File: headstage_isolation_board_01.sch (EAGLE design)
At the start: 55 parts, among them J1 DC_POWER_JACK-PJ-102AH

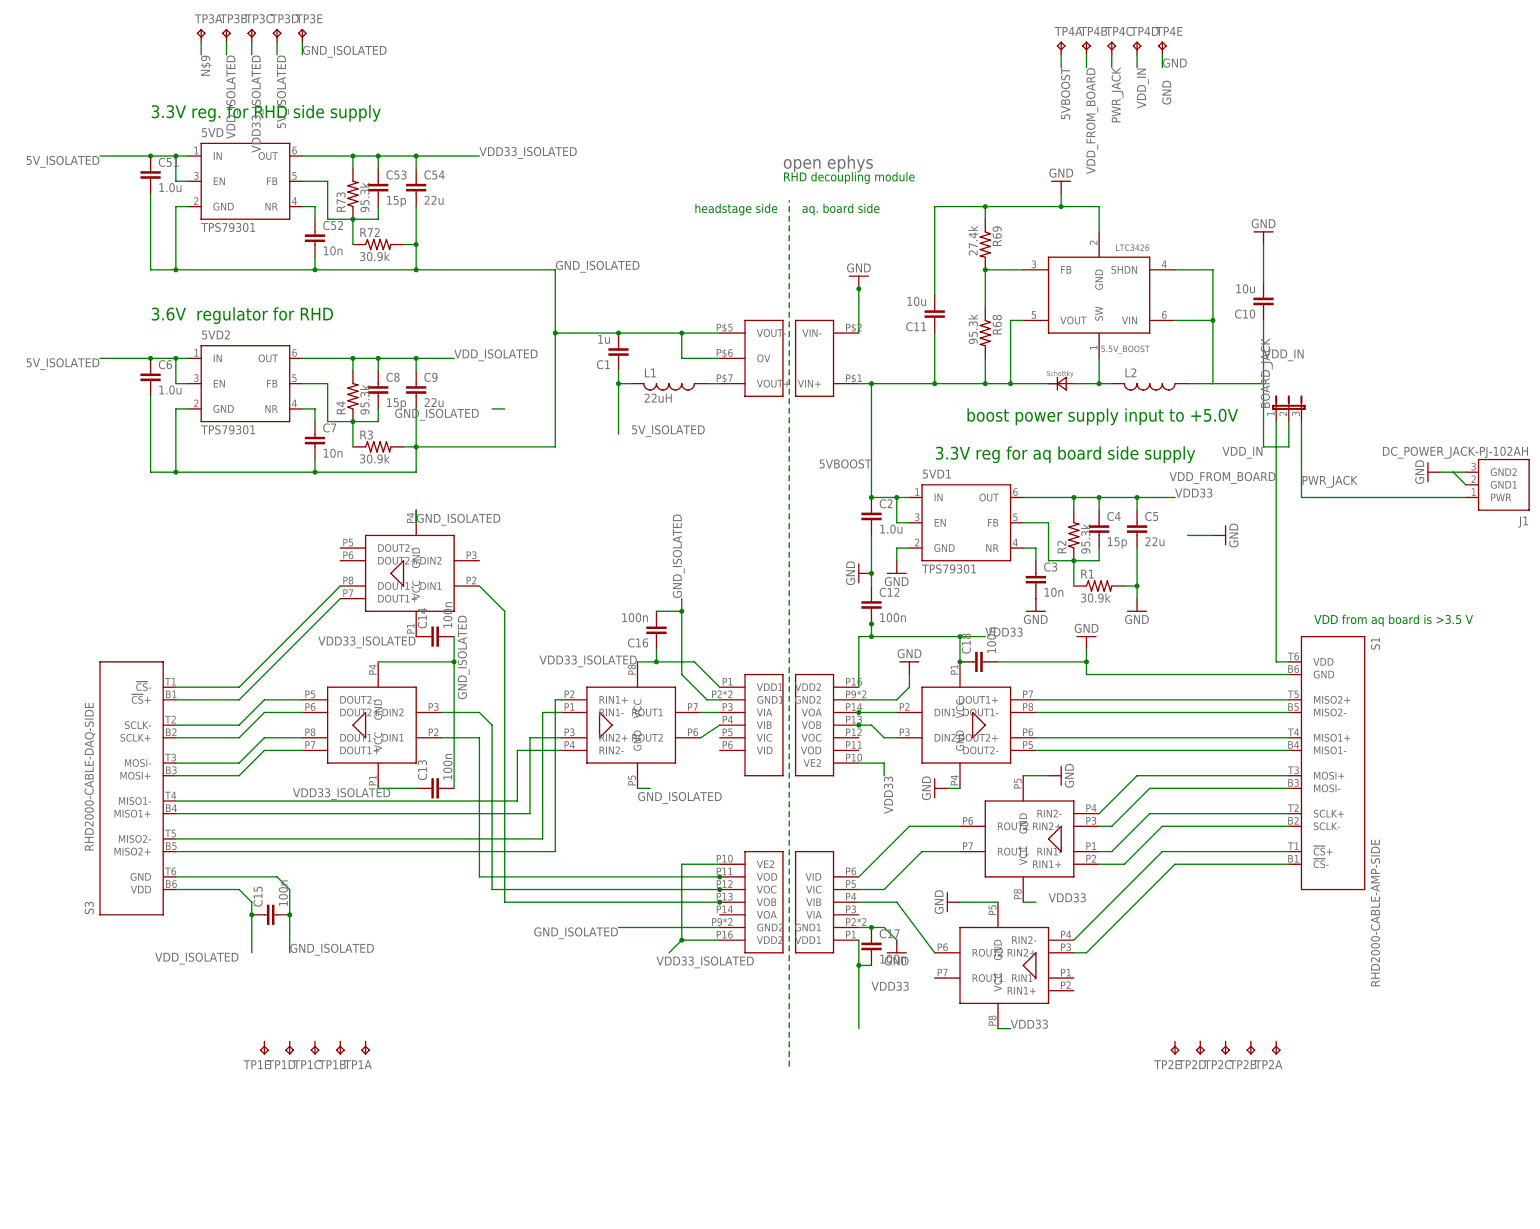
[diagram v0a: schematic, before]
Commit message: added all test points
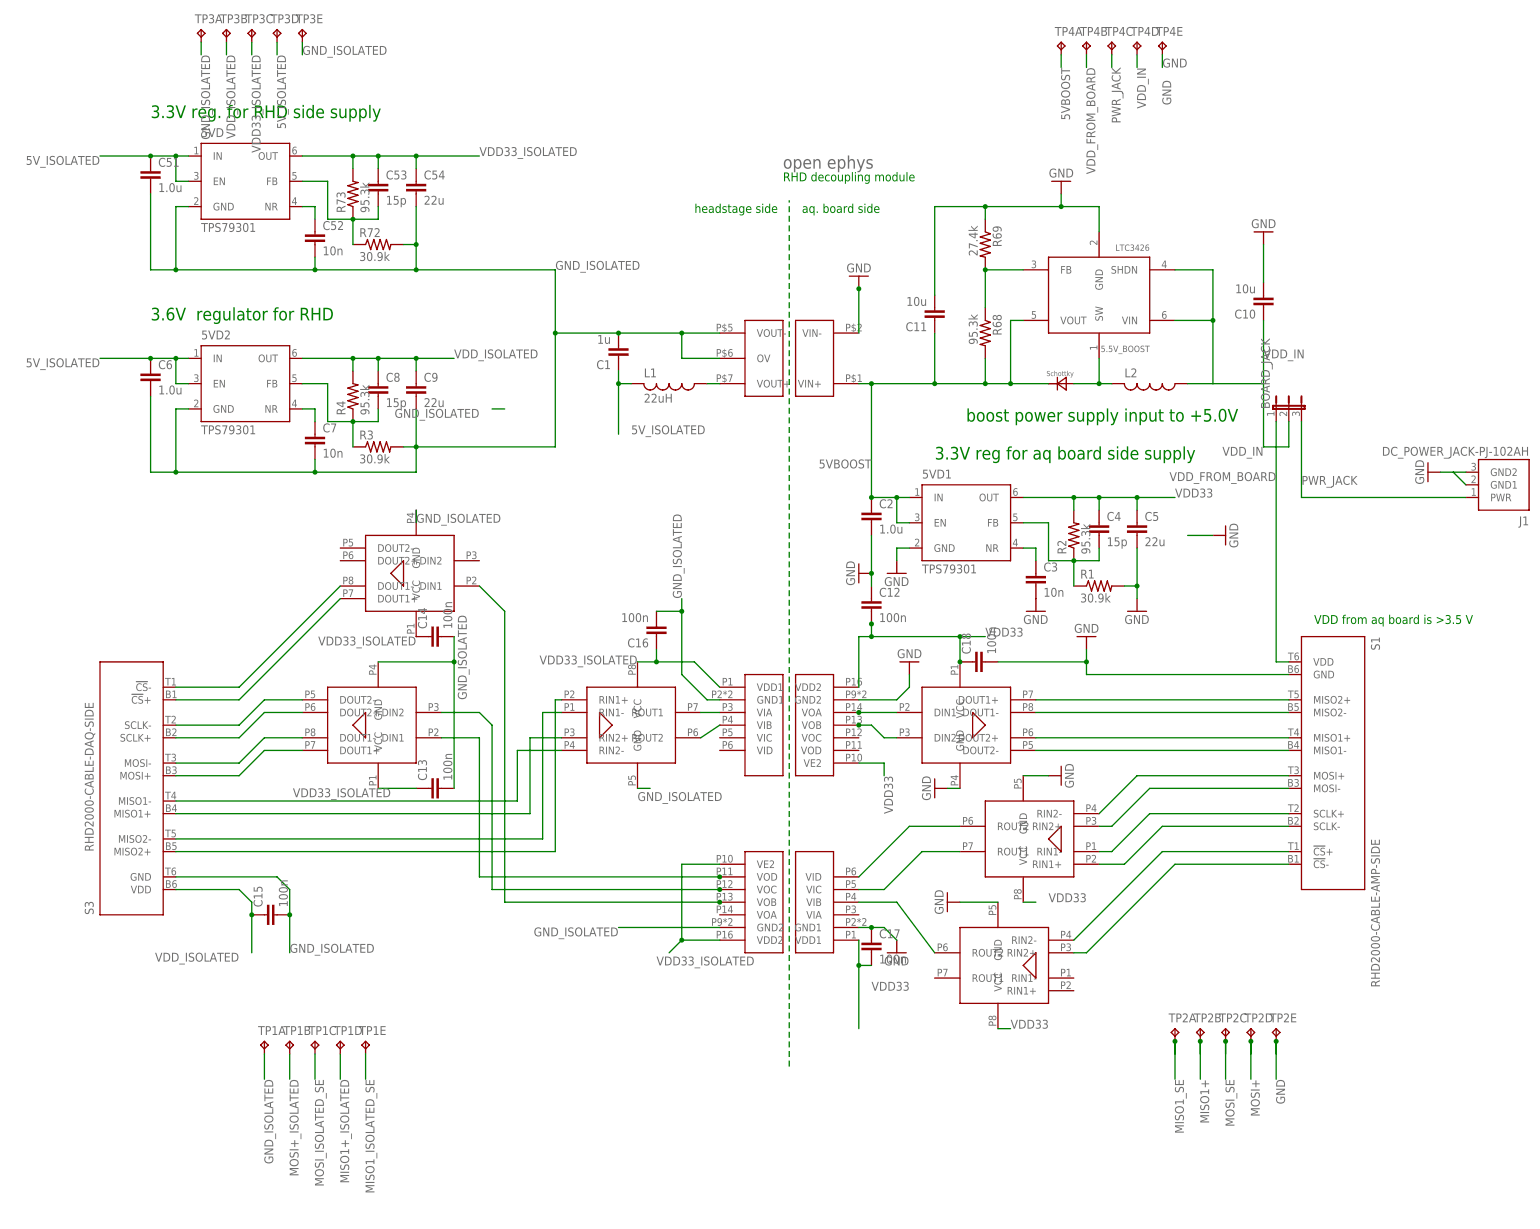
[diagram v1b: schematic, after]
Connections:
- net N$26 renamed SCLK_SE
- net N$27 renamed CS_SE
- net N$29 renamed SCLK_ISOLATED_SE
- net N$30 renamed CS_ISOLATED_SE
- net N$5 renamed MISO2_SE
- net N$7 renamed MISO2_ISOLATED_SE
- removed net N$25: U$2.VID, U$7.ROUT2
- removed net N$28: U$2.VOD, U$5.DIN1
- removed net N$6: U$10.VOB, U$4.DIN2
- removed net N$8: U$10.VIB, U$6.ROUT2
- removed net N$9: TP3A.TP
- new net MISO1_ISOLATED_SE: TP1E.TP, U$10.VIB, U$6.ROUT2
- new net MISO1_SE: TP2A.TP, U$10.VOB, U$4.DIN2
- new net MOSI_ISOLATED_SE: TP1C.TP, U$2.VOD, U$5.DIN1
- new net MOSI_SE: TP2C.TP, U$2.VID, U$7.ROUT2
- net GND: now also TP2E.TP
- net GND_ISOLATED: now also TP1A.TP, TP3A.TP
- net MISO1+: now also TP2B.TP
- net MISO1+_ISOLATED: now also TP1D.TP
- net MOSI+: now also TP2D.TP
- net MOSI+_ISOLATED: now also TP1B.TP
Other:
- moved on the sheet: TP1A, TP1B, TP1C, TP1D, TP1E, TP2A, TP2B, TP2C, TP2D, TP2E
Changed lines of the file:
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@@
 <part name="C18" library="RHD2000_eval_board" deviceset="C" device="_0603" value="100n"/>
 <part name="S3" library="RHD2000_eval_board" deviceset="RHD2000-CABLE-DAQ-SIDE" device=""/>
-<part name="TP1" library="testpad" deviceset="TP5" device="P5-25-13"/>
-<part name="TP2" library="testpad" deviceset="TP5" device="P5-25-13"/>
 <part name="TP3" library="testpad" deviceset="TP5" device="P5-25-13"/>
 <part name="TP4" library="testpad" deviceset="TP5" device="P5-25-13"/>
@@
 <part name="J1" library="RHD2000_eval_board" deviceset="DC_POWER_JACK" device="-PJ-102AH"/>
 <part name="GND12" library="supply1" deviceset="GND" device=""/>
+<part name="TP1" library="testpad" deviceset="TP5" device="P5-25-13"/>
+<part name="TP2" library="testpad" deviceset="TP5" device="P5-25-13"/>
 </parts>
 <sheets>
@@
 <instance part="C18" gate="C" x="99.06" y="-38.1" rot="R90"/>
 <instance part="S3" gate="A" x="-68.58" y="-63.5" rot="R270"/>
-<instance part="TP1" gate="A" x="-22.86" y="-116.84" rot="R180"/>
-<instance part="TP1" gate="B" x="-27.94" y="-116.84" rot="R180"/>
-<instance part="TP1" gate="C" x="-33.02" y="-116.84" rot="R180"/>
-<instance part="TP1" gate="D" x="-38.1" y="-116.84" rot="R180"/>
-<instance part="TP1" gate="E" x="-43.18" y="-116.84" rot="R180"/>
-<instance part="TP2" gate="A" x="160.02" y="-116.84" rot="R180"/>
-<instance part="TP2" gate="B" x="154.94" y="-116.84" rot="R180"/>
-<instance part="TP2" gate="C" x="149.86" y="-116.84" rot="R180"/>
-<instance part="TP2" gate="D" x="144.78" y="-116.84" rot="R180"/>
-<instance part="TP2" gate="E" x="139.7" y="-116.84" rot="R180"/>
 <instance part="TP3" gate="A" x="-55.88" y="88.9"/>
 <instance part="TP3" gate="B" x="-50.8" y="88.9"/>
@@
 <instance part="J1" gate="A" x="205.74" y="-2.54" rot="R180"/>
 <instance part="GND12" gate="1" x="190.5" y="0" rot="R270"/>
+<instance part="TP1" gate="A" x="-43.18" y="-114.3"/>
+<instance part="TP1" gate="B" x="-38.1" y="-114.3"/>
+<instance part="TP1" gate="C" x="-33.02" y="-114.3"/>
+<instance part="TP1" gate="D" x="-27.94" y="-114.3"/>
+<instance part="TP1" gate="E" x="-22.86" y="-114.3"/>
+<instance part="TP2" gate="A" x="139.7" y="-111.76"/>
+<instance part="TP2" gate="B" x="144.78" y="-111.76"/>
+<instance part="TP2" gate="C" x="149.86" y="-111.76"/>
+<instance part="TP2" gate="D" x="154.94" y="-111.76"/>
+<instance part="TP2" gate="E" x="160.02" y="-111.76"/>
 </instances>
 <busses>
@@
 <wire x1="111.76" y1="-53.34" x2="162.56" y2="-53.34" width="0.1524" layer="91"/>
 </segment>
+<segment>
+<wire x1="144.78" y1="-116.84" x2="144.78" y2="-114.3" width="0.1524" layer="91"/>
+<label x="144.78" y="-121.92" size="1.778" layer="95" rot="R270"/>
+<pinref part="TP2" gate="B" pin="TP"/>
+<wire x1="144.78" y1="-114.3" x2="144.78" y2="-121.92" width="0.1524" layer="91"/>
+<junction x="144.78" y="-114.3"/>
+</segment>
 </net>
 <net name="MISO1-" class="0">
@@
 </segment>
 </net>
-<net name="N$5" class="0">
+<net name="MISO2_SE" class="0">
 <segment>
 <pinref part="U$4" gate="G$1" pin="DIN1"/>
@@
 </segment>
 </net>
-<net name="N$6" class="0">
+<net name="MISO1_SE" class="0">
 <segment>
 <pinref part="U$4" gate="G$1" pin="DIN2"/>
@@
 <junction x="76.2" y="-50.8"/>
 </segment>
-</net>
-<net name="N$7" class="0">
+<segment>
+<wire x1="139.7" y1="-116.84" x2="139.7" y2="-114.3" width="0.1524" layer="91"/>
+<label x="139.7" y="-121.92" size="1.778" layer="95" rot="R270"/>
+<pinref part="TP2" gate="A" pin="TP"/>
+<wire x1="139.7" y1="-114.3" x2="139.7" y2="-121.92" width="0.1524" layer="91"/>
+<junction x="139.7" y="-114.3"/>
+</segment>
+</net>
+<net name="MISO2_ISOLATED_SE" class="0">
 <segment>
 <pinref part="U$6" gate="G$1" pin="ROUT1"/>
@@
 </segment>
 </net>
-<net name="N$8" class="0">
+<net name="MISO1_ISOLATED_SE" class="0">
 <segment>
 <pinref part="U$6" gate="G$1" pin="ROUT2"/>
 <wire x1="48.26" y1="-50.8" x2="44.45" y2="-53.34" width="0.1524" layer="91"/>
 <pinref part="U$10" gate="G$1" pin="VIB"/>
+</segment>
+<segment>
+<wire x1="-22.86" y1="-116.84" x2="-22.86" y2="-121.92" width="0.1524" layer="91"/>
+<label x="-22.86" y="-121.92" size="1.778" layer="95" rot="R270"/>
+<pinref part="TP1" gate="E" pin="TP"/>
 </segment>
 </net>
@@
 <pinref part="S3" gate="A" pin="MISO1+"/>
 </segment>
+<segment>
+<wire x1="-27.94" y1="-116.84" x2="-27.94" y2="-121.92" width="0.1524" layer="91"/>
+<label x="-27.94" y="-121.92" size="1.778" layer="95" rot="R270"/>
+<pinref part="TP1" gate="D" pin="TP"/>
+</segment>
 </net>
 <net name="MISO1-_ISOLATED" class="0">
@@
 <pinref part="U$7" gate="G$1" pin="RIN2-"/>
 </segment>
+<segment>
+<wire x1="154.94" y1="-116.84" x2="154.94" y2="-114.3" width="0.1524" layer="91"/>
+<label x="154.94" y="-121.92" size="1.778" layer="95" rot="R270"/>
+<pinref part="TP2" gate="D" pin="TP"/>
+<wire x1="154.94" y1="-114.3" x2="154.94" y2="-121.92" width="0.1524" layer="91"/>
+<junction x="154.94" y="-114.3"/>
+</segment>
 </net>
 <net name="CS-" class="0">
@@
 </segment>
 </net>
-<net name="N$28" class="0">
+<net name="MOSI_ISOLATED_SE" class="0">
 <segment>
 <wire x1="-7.62" y1="-53.34" x2="0" y2="-53.34" width="0.1524" layer="91"/>
@@
 <junction x="48.26" y="-81.28"/>
 </segment>
-</net>
-<net name="N$29" class="0">
+<segment>
+<wire x1="-33.02" y1="-116.84" x2="-33.02" y2="-121.92" width="0.1524" layer="91"/>
+<label x="-33.02" y="-121.92" size="1.778" layer="95" rot="R270"/>
+<pinref part="TP1" gate="C" pin="TP"/>
+</segment>
+</net>
+<net name="SCLK_ISOLATED_SE" class="0">
 <segment>
 <wire x1="48.26" y1="-83.82" x2="2.54" y2="-83.82" width="0.1524" layer="91"/>
@@
 </segment>
 </net>
-<net name="N$30" class="0">
+<net name="CS_ISOLATED_SE" class="0">
 <segment>
 <wire x1="48.26" y1="-86.36" x2="5.08" y2="-86.36" width="0.1524" layer="91"/>
@@
 <wire x1="-48.26" y1="-60.96" x2="-60.96" y2="-60.96" width="0.1524" layer="91"/>
 </segment>
-</net>
-<net name="N$25" class="0">
+<segment>
+<wire x1="-38.1" y1="-116.84" x2="-38.1" y2="-121.92" width="0.1524" layer="91"/>
+<label x="-38.1" y="-121.92" size="1.778" layer="95" rot="R270"/>
+<pinref part="TP1" gate="B" pin="TP"/>
+</segment>
+</net>
+<net name="MOSI_SE" class="0">
 <segment>
 <wire x1="76.2" y1="-81.28" x2="86.36" y2="-71.12" width="0.1524" layer="91"/>
@@
 <pinref part="U$2" gate="G$1" pin="VID"/>
 </segment>
-</net>
-<net name="N$26" class="0">
+<segment>
+<wire x1="149.86" y1="-116.84" x2="149.86" y2="-114.3" width="0.1524" layer="91"/>
+<label x="149.86" y="-121.92" size="1.778" layer="95" rot="R270"/>
+<pinref part="TP2" gate="C" pin="TP"/>
+<wire x1="149.86" y1="-114.3" x2="149.86" y2="-121.92" width="0.1524" layer="91"/>
+<junction x="149.86" y="-114.3"/>
+</segment>
+</net>
+<net name="SCLK_SE" class="0">
 <segment>
 <pinref part="U$7" gate="G$1" pin="ROUT1"/>
@@
 </segment>
 </net>
-<net name="N$27" class="0">
+<net name="CS_SE" class="0">
 <segment>
 <pinref part="U$8" gate="G$1" pin="ROUT2"/>
@@
 <label x="-35.56" y="83.82" size="1.778" layer="95"/>
 </segment>
+<segment>
+<wire x1="-43.18" y1="-116.84" x2="-43.18" y2="-121.92" width="0.1524" layer="91"/>
+<label x="-43.18" y="-121.92" size="1.778" layer="95" rot="R270"/>
+<pinref part="TP1" gate="A" pin="TP"/>
+</segment>
+<segment>
+<pinref part="TP3" gate="A" pin="TP"/>
+<wire x1="-55.88" y1="86.36" x2="-55.88" y2="83.82" width="0.1524" layer="91"/>
+<label x="-55.88" y="83.82" size="1.778" layer="95" rot="R270"/>
+</segment>
 </net>
 <net name="VDD_ISOLATED" class="0">
@@
 <wire x1="195.58" y1="0" x2="193.04" y2="0" width="0.1524" layer="91"/>
 <pinref part="GND12" gate="1" pin="GND"/>
+</segment>
+<segment>
+<wire x1="160.02" y1="-116.84" x2="160.02" y2="-114.3" width="0.1524" layer="91"/>
+<label x="160.02" y="-121.92" size="1.778" layer="95" rot="R270"/>
+<pinref part="TP2" gate="E" pin="TP"/>
+<wire x1="160.02" y1="-114.3" x2="160.02" y2="-121.92" width="0.1524" layer="91"/>
+<junction x="160.02" y="-114.3"/>
 </segment>
 </net>
@@
 </segment>
 </net>
-<net name="N$9" class="0">
-<segment>
-<pinref part="TP3" gate="A" pin="TP"/>
-<wire x1="-55.88" y1="86.36" x2="-55.88" y2="83.82" width="0.1524" layer="91"/>
-<label x="-55.88" y="83.82" size="1.778" layer="95" rot="R270"/>
-</segment>
-</net>

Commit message: added LVDS termination resistors
should fix bug #2
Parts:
- added R5, R6: 100, RHD2000_eval_board:R_0603
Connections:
- net MISO1+_ISOLATED: now also R6.1
- net MISO1-_ISOLATED: now also R6.2
- net MISO2+_ISOLATED: now also R5.1
- net MISO2-_ISOLATED: now also R5.2
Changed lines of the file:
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@@
 <part name="TP1" library="testpad" deviceset="TP5" device="P5-25-13"/>
 <part name="TP2" library="testpad" deviceset="TP5" device="P5-25-13"/>
+<part name="R5" library="RHD2000_eval_board" deviceset="R" device="_0603" value="100"/>
+<part name="R6" library="RHD2000_eval_board" deviceset="R" device="_0603" value="100"/>
 </parts>
 <sheets>
@@
 <instance part="TP2" gate="D" x="154.94" y="-111.76"/>
 <instance part="TP2" gate="E" x="160.02" y="-111.76"/>
+<instance part="R5" gate="R" x="-25.4" y="-81.28"/>
+<instance part="R6" gate="R" x="-12.7" y="-81.28"/>
 </instances>
 <busses>
@@
 <wire x1="16.51" y1="-48.26" x2="12.7" y2="-48.26" width="0.1524" layer="91"/>
 <wire x1="12.7" y1="-48.26" x2="12.7" y2="-73.66" width="0.1524" layer="91"/>
-<wire x1="12.7" y1="-73.66" x2="-60.96" y2="-73.66" width="0.1524" layer="91"/>
+<wire x1="12.7" y1="-73.66" x2="-20.32" y2="-73.66" width="0.1524" layer="91"/>
 <pinref part="S3" gate="A" pin="MISO2-"/>
+<pinref part="R5" gate="R" pin="2"/>
+<wire x1="-20.32" y1="-73.66" x2="-60.96" y2="-73.66" width="0.1524" layer="91"/>
+<wire x1="-20.32" y1="-81.28" x2="-20.32" y2="-73.66" width="0.1524" layer="91"/>
+<junction x="-20.32" y="-73.66"/>
 </segment>
 </net>
@@
 <wire x1="16.51" y1="-53.34" x2="10.16" y2="-53.34" width="0.1524" layer="91"/>
 <wire x1="10.16" y1="-53.34" x2="10.16" y2="-68.58" width="0.1524" layer="91"/>
-<wire x1="10.16" y1="-68.58" x2="-60.96" y2="-68.58" width="0.1524" layer="91"/>
+<wire x1="10.16" y1="-68.58" x2="-17.78" y2="-68.58" width="0.1524" layer="91"/>
 <pinref part="S3" gate="A" pin="MISO1+"/>
+<pinref part="R6" gate="R" pin="1"/>
+<wire x1="-17.78" y1="-68.58" x2="-60.96" y2="-68.58" width="0.1524" layer="91"/>
+<wire x1="-17.78" y1="-81.28" x2="-17.78" y2="-68.58" width="0.1524" layer="91"/>
+<junction x="-17.78" y="-68.58"/>
 </segment>
 <segment>
@@
 <wire x1="7.62" y1="-55.88" x2="16.51" y2="-55.88" width="0.1524" layer="91"/>
 <wire x1="7.62" y1="-55.88" x2="7.62" y2="-66.04" width="0.1524" layer="91"/>
-<wire x1="7.62" y1="-66.04" x2="-60.96" y2="-66.04" width="0.1524" layer="91"/>
+<wire x1="7.62" y1="-66.04" x2="-7.62" y2="-66.04" width="0.1524" layer="91"/>
 <pinref part="S3" gate="A" pin="MISO1-"/>
+<pinref part="R6" gate="R" pin="2"/>
+<wire x1="-7.62" y1="-66.04" x2="-60.96" y2="-66.04" width="0.1524" layer="91"/>
+<wire x1="-7.62" y1="-81.28" x2="-7.62" y2="-66.04" width="0.1524" layer="91"/>
+<junction x="-7.62" y="-66.04"/>
 </segment>
 </net>
 <net name="MISO2+_ISOLATED" class="0">
 <segment>
-<wire x1="-60.96" y1="-76.2" x2="15.24" y2="-76.2" width="0.1524" layer="91"/>
+<wire x1="-60.96" y1="-76.2" x2="-30.48" y2="-76.2" width="0.1524" layer="91"/>
+<wire x1="-30.48" y1="-76.2" x2="15.24" y2="-76.2" width="0.1524" layer="91"/>
 <wire x1="15.24" y1="-76.2" x2="15.24" y2="-45.72" width="0.1524" layer="91"/>
 <pinref part="U$6" gate="G$1" pin="RIN1+"/>
 <wire x1="15.24" y1="-45.72" x2="16.51" y2="-45.72" width="0.1524" layer="91"/>
 <pinref part="S3" gate="A" pin="MISO2+"/>
-</segment>
-</net>
+<pinref part="R5" gate="R" pin="1"/>
+<wire x1="-30.48" y1="-81.28" x2="-30.48" y2="-76.2" width="0.1524" layer="91"/>
+<junction x="-30.48" y="-76.2"/>
+</segment>
+</net>
